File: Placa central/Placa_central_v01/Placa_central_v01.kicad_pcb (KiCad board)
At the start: 2 copper layers, 36 parts, among them J1 Conn_8.4V_PlacaAlimentação, J16 Conn_01x01_Motor1PonteHPCB, J2 Conn_01x02_ArduinoTxRx, J26 Conn_02x08_Odd_Even, J27 Conn_01x01_Motor2PonteHPCB, J28 Conn_01x01_Motor1PCBMotor, J29 Conn_01x01_Motor2PCBMotor, J3 Conn_01x01_ArduinoReset, J37 Conn_01x01_8.4VPonteH, J38 Conn_01x01_5VPonteH, J39 Conn_01x01_GNDPonteH, J4 Conn_GND_PlacaAlimentação, J40 Conn_01x01_Motor1PWM, J41 Conn_01x01_Motor1Dir1, J42 Conn_01x01_Motor1Dir2, J43 Conn_01x01_Motor2Dir1, J44 Conn_01x01_Motor2Dir2, J45 Conn_01x01_Motor2PWM, J48 Conn_01x01_5VEncoderEsq, J49 Conn_01x01_OutputEncoderEsq, J50 Conn_01x01_GNDEncoderEsq, J51 Conn_01x01_5VEncoderDir, J52 Conn_01x01_OutputEncoderDir, J53 Conn_01x01_GNDEncoderDir, SW3 SW_comando1

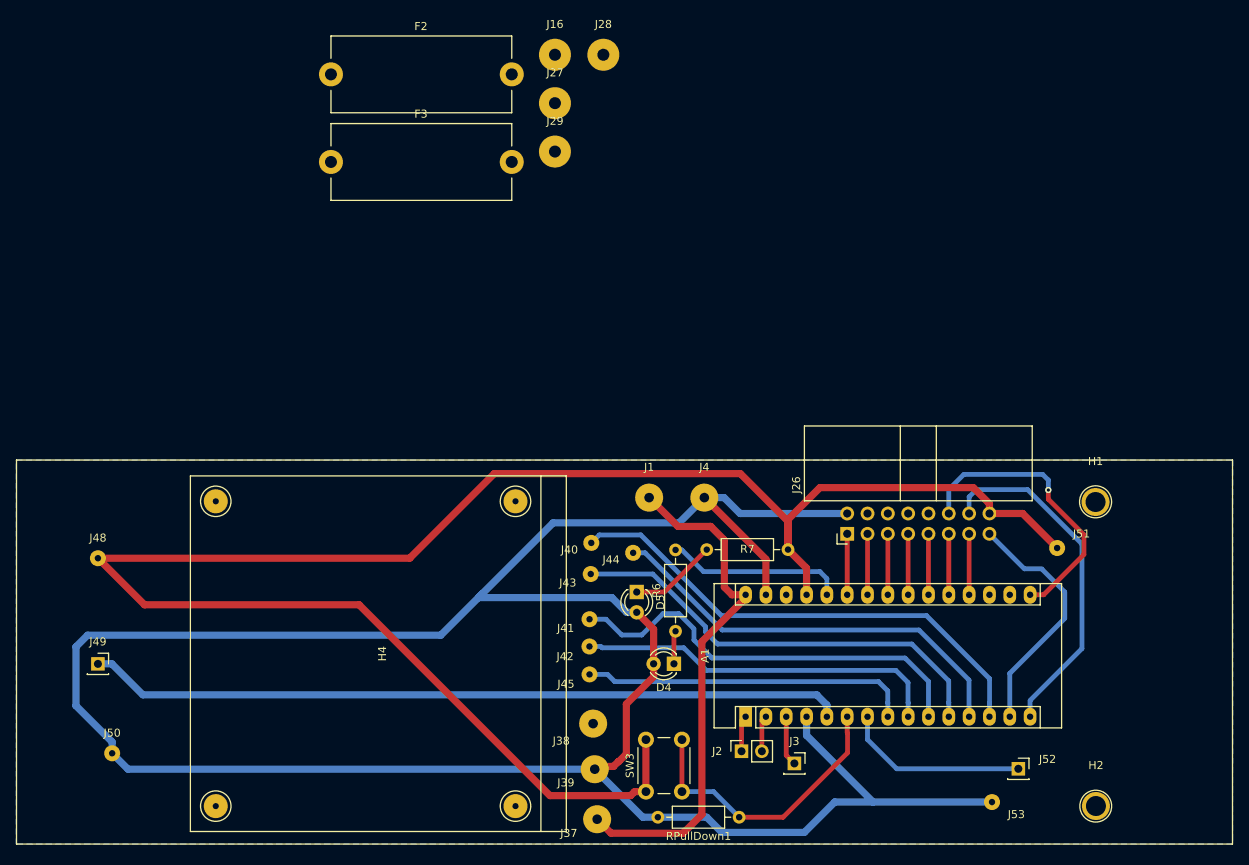
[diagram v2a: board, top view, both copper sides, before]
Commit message: Preparação da placa encoder para impressão
E mexido na placa central: adicionado gnd na placa de cima e keep out area
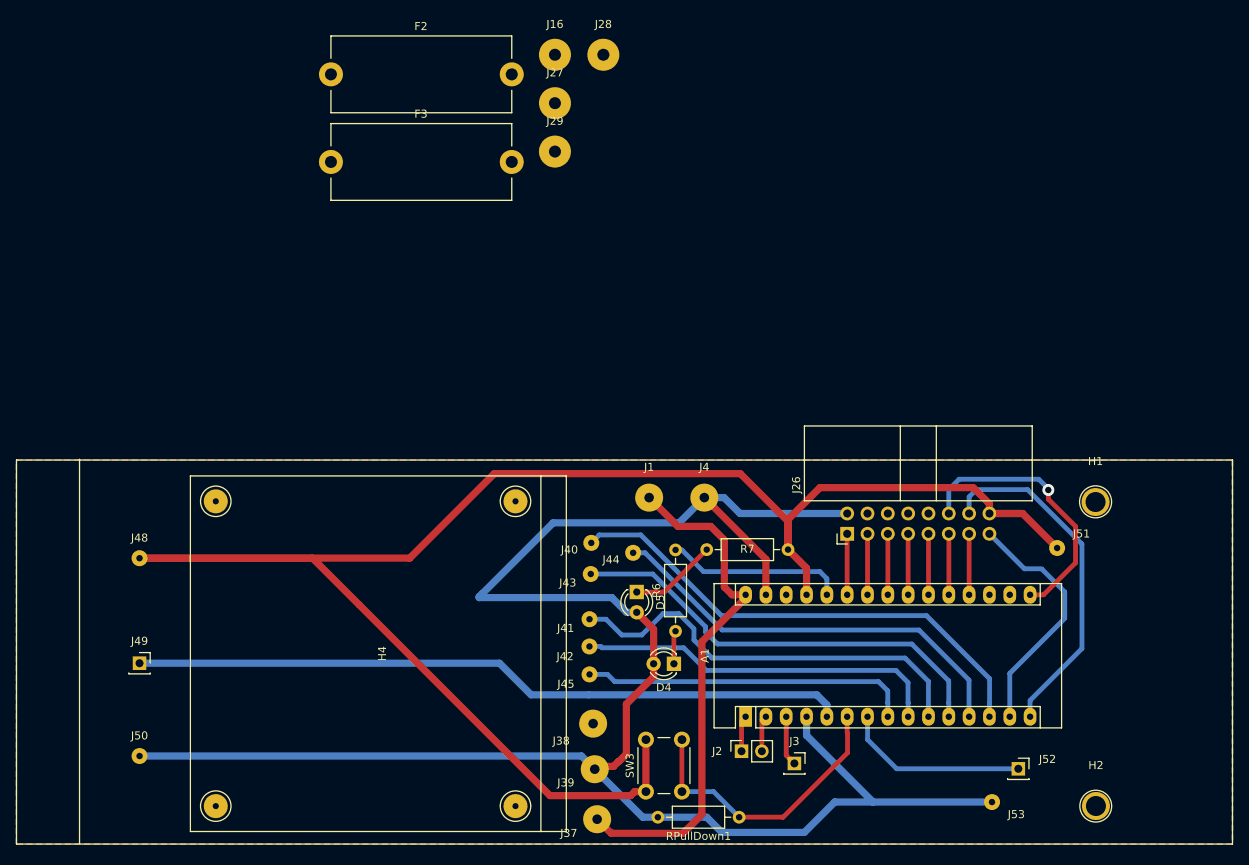
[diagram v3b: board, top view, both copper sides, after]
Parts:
- moved J49 5.20 mm to (40.0, 148.0)
- moved J48 5.20 mm to (40.0, 134.9)
- moved J50 3.44 mm to (40.0, 159.6)
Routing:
- net GND: track 311.1 -> 238.8 mm
- net 5VArduino: track 233.7 -> 223.2 mm
- net Encoder1: track 94.7 -> 89.5 mm
- net ArduinoD13: track 36.5 -> 34.5 mm
- added copper zone on F.Cu, net GND
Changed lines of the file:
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@@
-(kicad_pcb (version 20171130) (host pcbnew 5.1.4-e60b266~84~ubuntu18.04.1)
+(kicad_pcb (version 20171130) (host pcbnew "(5.1.2)-2")
   (general
     (thickness 1.6)
-    (drawings 6)
-    (tracks 198)
+    (drawings 7)
+    (tracks 193)
     (zones 0)
     (modules 36)
@@
   )
   (module Connector_Wire:SolderWirePad_1x01_Drill0.8mm (layer F.Cu)
-    (at 34.798 134.874)
+    (at 40 134.874)
     (descr "Wire solder connection")
     (tags connector)
@@
   )
   (module Connector_PinSocket_2.54mm:PinSocket_1x01_P2.54mm_Vertical (layer F.Cu)
-    (at 34.798 148.082)
+    (at 40 148)
     (descr "Through hole straight socket strip, 1x01, 2.54mm pitch, single row (from Kicad 4.0.7), script generated")
     (tags "Through hole socket strip THT 1x01 2.54mm single row")
@@
   )
   (module Connector_Wire:SolderWirePad_1x01_Drill0.8mm (layer F.Cu)
-    (at 36.576 159.258)
+    (at 40 159.6)
     (descr "Wire solder connection")
     (tags connector)
@@
     (pad 1 thru_hole circle (at 0 0) (size 3.5 3.5) (drill 2.49936) (layers *.Cu *.Mask))
   )
+  (gr_line (start 32.5 122.5) (end 32.5 170.5) (layer F.SilkS) (width 0.12))
   (gr_line (start 24.61768 170.60536) (end 24.61768 122.6019) (layer F.SilkS) (width 0.12))
   (gr_line (start 176.6189 170.60536) (end 24.61768 170.60536) (layer F.SilkS) (width 0.12))
@@
   (segment (start 126.904 160.562) (end 131.696 165.354) (width 0.9) (layer B.Cu) (net 7))
   (segment (start 131.696 165.354) (end 146.558 165.354) (width 0.9) (layer B.Cu) (net 7))
-  (segment (start 38.568 161.25) (end 36.576 159.258) (width 0.9) (layer B.Cu) (net 7))
-  (segment (start 96.9 161.25) (end 38.568 161.25) (width 0.9) (layer B.Cu) (net 7))
   (segment (start 100.877208 141.64) (end 99.037208 139.8) (width 0.9) (layer B.Cu) (net 7))
   (segment (start 102.15 141.64) (end 100.877208 141.64) (width 0.9) (layer B.Cu) (net 7))
@@
   (segment (start 107.45 130.45) (end 91.7 130.45) (width 0.9) (layer B.Cu) (net 7))
   (segment (start 99.037208 139.8) (end 82.45 139.8) (width 0.9) (layer B.Cu) (net 7))
-  (segment (start 77.65 144.5) (end 82.8429 139.3071) (width 0.9) (layer B.Cu) (net 7))
-  (segment (start 33.5 144.5) (end 77.65 144.5) (width 0.9) (layer B.Cu) (net 7))
   (segment (start 91.7 130.45) (end 82.8429 139.3071) (width 0.9) (layer B.Cu) (net 7))
   (segment (start 82.8429 139.3071) (end 82.45 139.7) (width 0.9) (layer B.Cu) (net 7))
-  (segment (start 32.05 153.318508) (end 32.05 145.95) (width 0.9) (layer B.Cu) (net 7))
-  (segment (start 36.576 159.258) (end 36.576 157.844508) (width 0.9) (layer B.Cu) (net 7))
-  (segment (start 36.576 157.844508) (end 32.05 153.318508) (width 0.9) (layer B.Cu) (net 7))
-  (segment (start 32.05 145.95) (end 33.5 144.5) (width 0.9) (layer B.Cu) (net 7))
+  (segment (start 95.25 159.6) (end 96.9 161.25) (width 0.9) (layer B.Cu) (net 7))
+  (segment (start 40 159.6) (end 95.25 159.6) (width 0.9) (layer B.Cu) (net 7))
   (segment (start 141.158 131.826) (end 141.158 139.446) (width 0.6) (layer F.Cu) (net 8))
-  (segment (start 40.416 151.95) (end 36.548 148.082) (width 0.9) (layer B.Cu) (net 9))
-  (segment (start 124.65 151.95) (end 40.416 151.95) (width 0.9) (layer B.Cu) (net 9))
-  (segment (start 125.918 153.218) (end 124.65 151.95) (width 0.9) (layer B.Cu) (net 9))
-  (segment (start 36.548 148.082) (end 34.798 148.082) (width 0.9) (layer B.Cu) (net 9))
+  (segment (start 85 148) (end 88.95 151.95) (width 0.9) (layer B.Cu) (net 9))
+  (segment (start 40 148) (end 85 148) (width 0.9) (layer B.Cu) (net 9))
   (segment (start 125.918 154.686) (end 125.918 153.218) (width 0.9) (layer B.Cu) (net 9))
+  (segment (start 124.65 151.95) (end 125.918 153.218) (width 0.9) (layer B.Cu) (net 9))
+  (segment (start 96.155909 151.95) (end 88.95 151.95) (width 0.9) (layer B.Cu) (net 9))
+  (segment (start 124.65 151.95) (end 96.155909 151.95) (width 0.9) (layer B.Cu) (net 9))
   (segment (start 138.618 131.826) (end 138.618 139.446) (width 0.6) (layer F.Cu) (net 10))
   (segment (start 130.998 157.551) (end 130.998 154.686) (width 0.6) (layer B.Cu) (net 11))
@@
   (segment (start 101.385787 164.55) (end 91.3 164.55) (width 0.9) (layer F.Cu) (net 21))
   (segment (start 91.3 164.55) (end 67.45 140.7) (width 0.9) (layer F.Cu) (net 21))
-  (segment (start 40.624 140.7) (end 34.798 134.874) (width 0.9) (layer F.Cu) (net 21))
-  (segment (start 67.45 140.7) (end 40.624 140.7) (width 0.9) (layer F.Cu) (net 21))
   (segment (start 123.378 136.118) (end 121.06 133.8) (width 0.9) (layer F.Cu) (net 21))
   (segment (start 123.378 139.446) (end 123.378 136.118) (width 0.9) (layer F.Cu) (net 21))
@@
   (segment (start 115.1 124.3) (end 121.06 130.26) (width 0.9) (layer F.Cu) (net 21))
   (segment (start 73.776 134.874) (end 84.35 124.3) (width 0.9) (layer F.Cu) (net 21))
-  (segment (start 34.798 134.874) (end 73.776 134.874) (width 0.9) (layer F.Cu) (net 21))
   (segment (start 84.35 124.3) (end 115.1 124.3) (width 0.9) (layer F.Cu) (net 21))
+  (segment (start 40 134.874) (end 73.776 134.874) (width 0.9) (layer F.Cu) (net 21))
+  (segment (start 61.624 134.874) (end 67.45 140.7) (width 0.9) (layer F.Cu) (net 21))
+  (segment (start 40 134.874) (end 61.624 134.874) (width 0.9) (layer F.Cu) (net 21))
   (segment (start 141.135045 154.686) (end 141.158 154.686) (width 0.6) (layer B.Cu) (net 22))
   (segment (start 141.158 152.961) (end 141.1478 152.9508) (width 0.6) (layer B.Cu) (net 22))
@@
   (segment (start 105.6 139.1) (end 110.9 133.8) (width 0.6) (layer F.Cu) (net 30))
   (segment (start 102.15 139.1) (end 105.6 139.1) (width 0.6) (layer F.Cu) (net 30))
-  (via (at 153.6 126.35) (size 0.8) (drill 0.4) (layers F.Cu B.Cu) (net 36))
+  (via (at 153.6 126.35) (size 1.5) (drill 0.8) (layers F.Cu B.Cu) (net 36))
   (segment (start 141.158 126.292) (end 141.158 129.286) (width 0.6) (layer B.Cu) (net 36))
-  (segment (start 143.05 124.4) (end 141.158 126.292) (width 0.6) (layer B.Cu) (net 36))
-  (segment (start 152.9 124.4) (end 143.05 124.4) (width 0.6) (layer B.Cu) (net 36))
+  (segment (start 142.45 125) (end 141.158 126.292) (width 0.6) (layer B.Cu) (net 36))
+  (segment (start 152.4 125) (end 142.45 125) (width 0.6) (layer B.Cu) (net 36))
+  (segment (start 153.6 126.35) (end 153.6 126.2) (width 0.6) (layer B.Cu) (net 36))
+  (segment (start 153.6 126.2) (end 152.4 125) (width 0.6) (layer B.Cu) (net 36))
   (segment (start 153.6 127.5) (end 153.6 126.35) (width 0.6) (layer F.Cu) (net 36))
-  (segment (start 158.05 131.95) (end 153.6 127.5) (width 0.6) (layer F.Cu) (net 36))
-  (segment (start 158.05 134.414) (end 158.05 131.95) (width 0.6) (layer F.Cu) (net 36))
+  (segment (start 157 130.9) (end 153.6 127.5) (width 0.6) (layer F.Cu) (net 36))
+  (segment (start 157 135.464) (end 157 130.9) (width 0.6) (layer F.Cu) (net 36))
   (segment (start 151.318 139.446) (end 153.018 139.446) (width 0.6) (layer F.Cu) (net 36))
-  (segment (start 153.018 139.446) (end 158.05 134.414) (width 0.6) (layer F.Cu) (net 36))
-  (segment (start 153.6 125.1) (end 152.9 124.4) (width 0.6) (layer B.Cu) (net 36))
-  (segment (start 153.6 126.35) (end 153.6 125.1) (width 0.6) (layer B.Cu) (net 36))
+  (segment (start 153.018 139.446) (end 157 135.464) (width 0.6) (layer F.Cu) (net 36))
   (zone (net 7) (net_name GND) (layer B.Cu) (hatch edge 0.508)
     (connect_pads (clearance 0.508))
@@
       )
     )
+  )
+  (zone (net 7) (net_name GND) (layer F.Cu) (hatch edge 0.508)
+    (connect_pads (clearance 0.508))
+    (min_thickness 0.254)
+    (fill (arc_segments 32) (thermal_gap 0.508) (thermal_bridge_width 0.508))
+    (polygon
+      (pts
+        (xy 24.6 122.6) (xy 176.6 122.6) (xy 176.6 170.6) (xy 24.6 170.6)
+      )
+    )
+  )
+  (zone (net 0) (net_name "") (layer F.Cu) (hatch edge 0.508)
+    (connect_pads (clearance 0.508))
+    (min_thickness 0.254)
+    (keepout (tracks allowed) (vias allowed) (copperpour not_allowed))
+    (fill (arc_segments 32) (thermal_gap 0.508) (thermal_bridge_width 0.508))
+    (polygon
+      (pts
+        (xy 46.6 124.8) (xy 89.8 124.8) (xy 89.8 168.6) (xy 46.6 168.6)
+      )
+    )

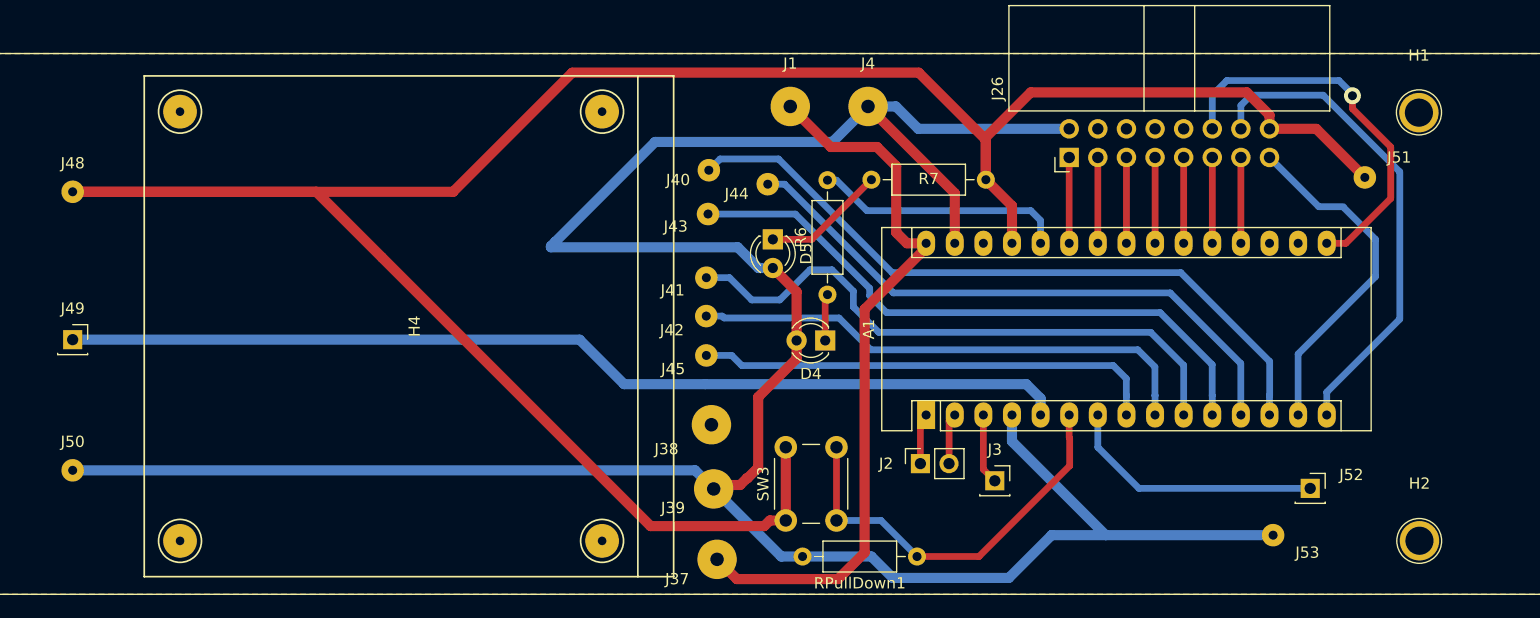
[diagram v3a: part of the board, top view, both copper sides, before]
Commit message: Pinos do conector alterados, conector agora está exclusivamente conectado na malha verde.
Criado net do Sensor8, quando houver a necessidade de utilizar a placa vermelha.
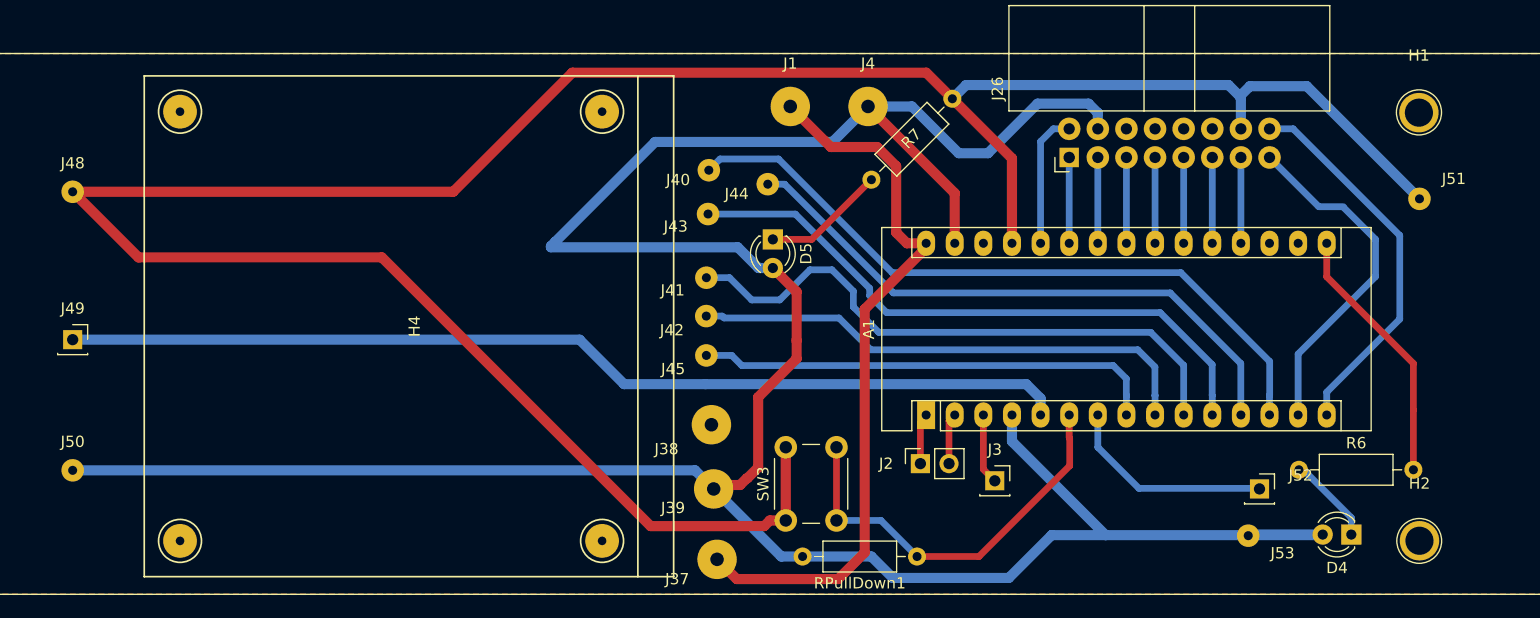
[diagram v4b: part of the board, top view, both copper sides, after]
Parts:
- moved D4 49.8 mm to (153.5, 165.3)
- moved R6 44.6 mm to (148.8, 159.6), turned to 0 degrees
- moved J51 5.21 mm to (159.6, 135.5)
- moved J52 4.50 mm to (145.3, 161.2)
- moved J53 2.21 mm to (144.3, 165.4)
- turned R7 to 45 degrees
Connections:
- A1 pad 16: ArduinoD13 -> LedAzul
- A1 pad 26: LedAzul -> Sensor8
- J26 pad 12: ArduinoD13 -> Net-(J26-Pad12)
- J26 pad 14: SensorDir -> 5VArduino
- J26 pad 16: 5VArduino -> SensorDir
- J26 pad 2: GND -> Sensor8
- J26 pad 4: Net-(J26-Pad4) -> GND
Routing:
- net ArduinoD13: track 34.5 -> 0.00 mm, vias 1 -> 0
- net GND: track 238.8 -> 256.9 mm
- net Sensor8: track 0.00 -> 12.0 mm
- net SensorDir: track 43.6 -> 34.1 mm
- net 5VArduino: track 223.2 -> 230.6 mm
- net Encoder2: track 23.2 -> 18.7 mm
- net Net-(D4-Pad1): track 4.16 -> 7.91 mm
- net LedAzul: track 22.4 -> 23.3 mm
